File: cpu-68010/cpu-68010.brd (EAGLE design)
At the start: 150 x 100 mm, 84 parts, among them IC10 74HC30D, IC11 74HC30D, IC12 74HC14D, IC13 MAX232, IC6 74HC00D, IC7 74HCT154DW, IC8 74HC04D, IC9 74HC148D, Q1 3.6864MHz, X1 FABC96R

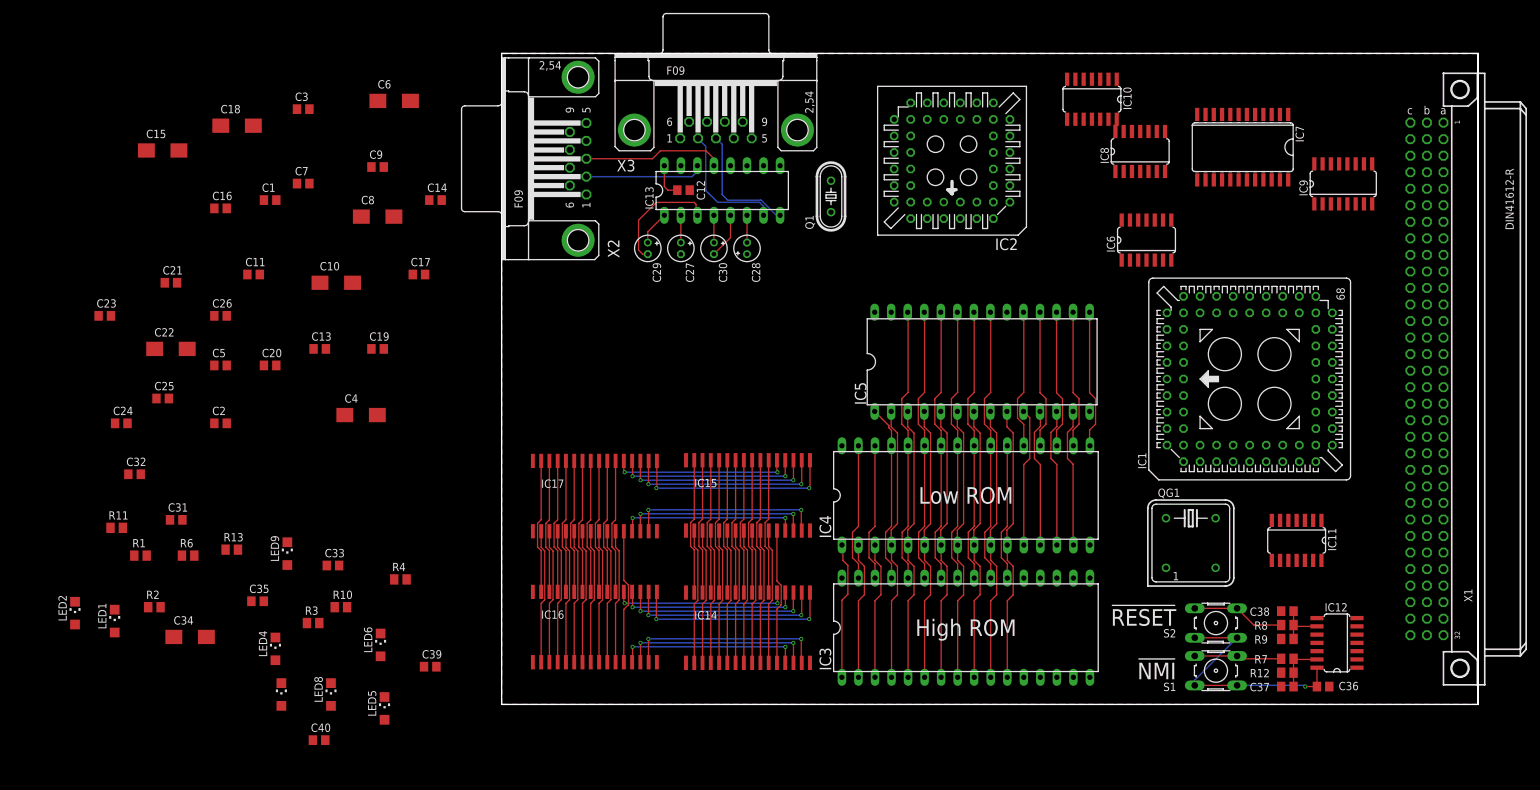
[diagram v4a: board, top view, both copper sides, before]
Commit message: routed remaining signals between SRAM, added decoupling chips and more status LEDs
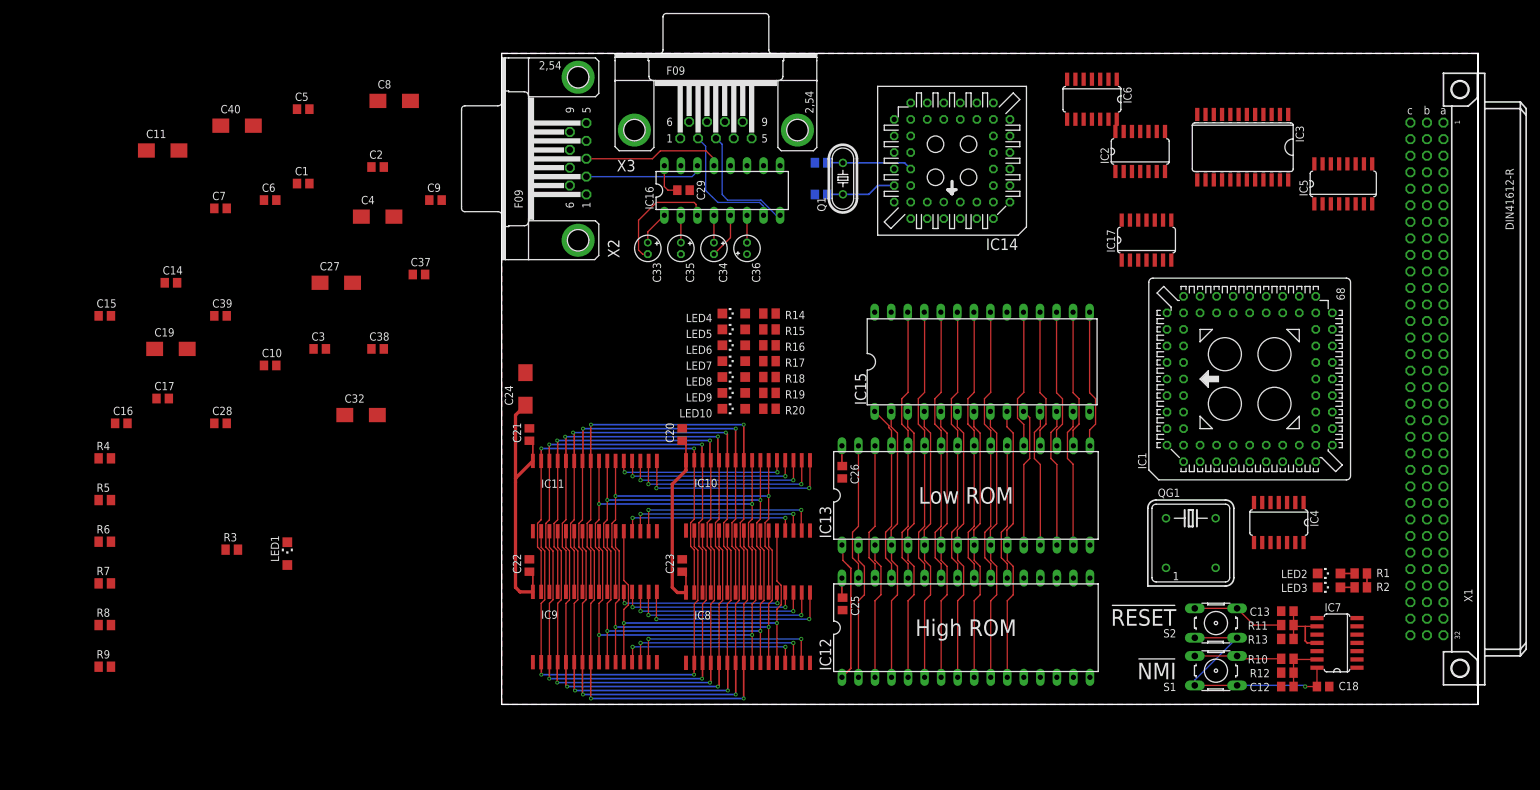
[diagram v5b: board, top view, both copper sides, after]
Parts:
- added LED10, LED7: YEL, led:CHIPLED_1206
- added R14, R15, R16, R17, R18, R19, R20: 680R, rcl:M0805
- added R5: 10k, rcl:M0805
- C10, C15, C18, C22, C6: value 47µF -> 100nF; device rcl:CT6032 -> rcl:C0805
- C11, C19, C24, C40: value 100nF -> 47µF; device rcl:C0805 -> rcl:CT6032
- C27: value 10µF -> 47µF; device rcl:E1,8-4 -> rcl:CT6032
- C28, C29: value 10µF -> 100nF; device rcl:E1,8-4 -> rcl:C0805
- C30: value 10µF -> 30pF; device rcl:E1,8-4 -> rcl:C0805
- C32: value 30pF -> 47µF; device rcl:C0805 -> rcl:CT6032
- C33, C35, C36: value 100nF -> 10µF; device rcl:C0805 -> rcl:E1,8-4
- C34: value 47µF -> 10µF; device rcl:CT6032 -> rcl:E1,8-4
- IC10, IC11: value 74HC30D -> (none); device 74xx-eu:SO14 -> 68komputer:SO32X
- IC12: value 74HC14D -> (none); device 74xx-eu:SO14 -> 68komputer:DIL32
- IC13: value MAX232 -> (none); device maxim:DIL16 -> 68komputer:DIL32
- IC14: device 68komputer:SO32X -> 68komputer:PLCC-S44
- IC15: device 68komputer:SO32X -> 68komputer:DIL28-6
- IC16: value (none) -> MAX232; device 68komputer:SO32X -> maxim:DIL16
- IC17: value (none) -> 74HC00D; device 68komputer:SO32X -> 74xx-eu:SO14
- IC2: value (none) -> 74HC04D; device 68komputer:PLCC-S44 -> 74xx-eu:SO14
- IC3: value (none) -> 74HCT154DW; device 68komputer:DIL32 -> 74xx-eu:SO24W
- IC4: value (none) -> 74HC30D; device 68komputer:DIL32 -> 74xx-eu:SO14
- IC5: value (none) -> 74HC148D; device 68komputer:DIL28-6 -> 74xx-eu:SO16
- IC6: value 74HC00D -> 74HC30D
- IC7: value 74HCT154DW -> 74HC14D; device 74xx-eu:SO24W -> 74xx-eu:SO14
- IC8: value 74HC04D -> (none); device 74xx-eu:SO14 -> 68komputer:SO32X
- IC9: value 74HC148D -> (none); device 74xx-eu:SO16 -> 68komputer:SO32X
- LED2, LED3: value GRN -> RED
- LED4, LED5, LED6, LED8, LED9: value GRN -> YEL
- R10, R11, R13, R4, R6: value 680R -> 10k
- moved LED2 192.7 mm to (127.1, 20.1), turned to 90 degrees
- moved C18 187.8 mm to (126.2, 2.74)
- moved R1 187.5 mm to (132.0, 20.1), turned to 180 degrees
- moved R2 185.3 mm to (132.0, 18.0), turned to 180 degrees
- moved R7 182.0 mm to (-61.0, 18.6), turned to 0 degrees
- moved R9 181.7 mm to (-61.0, 5.79), turned to 0 degrees
- moved R8 181.7 mm to (-61.0, 12.2), turned to 0 degrees
- moved R11 180.5 mm to (120.7, 12.2), turned to 180 degrees
- moved R13 162.7 mm to (120.7, 10.1), turned to 180 degrees
- moved LED3 161.8 mm to (127.1, 18.0), turned to 90 degrees
- moved C13 154.0 mm to (120.7, 14.3), turned to 180 degrees
- moved C37 147.7 mm to (-12.7, 66.0), turned to 0 degrees
- moved R10 145.6 mm to (120.7, 7.01), turned to 180 degrees
- moved C38 145.4 mm to (-19.1, 54.6), turned to 0 degrees
- moved IC9 133.6 mm to (14.3, 11.9)
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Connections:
- new net N$12: LED3.A, R2.2
- new net N$15: LED2.A, R1.2
- net !68681_CS: now also IC14.39, IC17.3; no longer IC2.39, IC6.3
- net !68681_DTACK: now also IC14.10, IC6.2, R9.2; no longer IC10.2, IC2.10
- net !68681_IRQ: now also IC14.24, IC5.2, R5.2; no longer IC2.24, IC9.2
- net !68681_IRQACK: now also IC14.41; no longer IC2.41
- net !A18: now also IC10.30, IC11.30, IC2.10, IC8.30, IC9.30; no longer IC14.30, IC15.30, IC16.30, IC17.30, IC8.10
- net !A19: now also IC17.2, IC2.6; no longer IC6.2, IC8.6
- net !DTACK: now also IC2.8; no longer IC8.8
- net !EXT_DTACK: now also IC6.1, R8.2; no longer IC10.1
- net !EXT_IRQ: now also IC5.1, R4.2; no longer IC9.1
- net !HALT: now also IC7.10, LED2.C
- net !IPL0: now also IC5.9; no longer IC9.9
- net !IPL1: now also IC5.7; no longer IC9.7
- net !IPL2: now also IC5.6; no longer IC9.6
- net !NMI: now also IC5.4, IC7.12, R7.2; no longer IC12.12, IC9.4
- net !OE: now also IC10.24, IC11.24, IC12.24, IC13.24, IC15.22, IC2.2, IC8.24, IC9.24; no longer IC14.24, IC15.24, IC16.24, IC17.24, IC3.24, IC4.24, IC5.22, IC8.2
- net !REGION0: now also IC12.22, IC13.22, IC3.1, IC6.3; no longer IC10.3, IC3.22, IC4.22, IC7.1
- net !REGION1: now also IC10.22, IC11.22, IC3.2, IC6.4, IC8.22, IC9.22; no longer IC10.4, IC14.22, IC15.22, IC16.22, IC17.22, IC7.2
- net !REGION10: now also IC3.11; no longer IC7.11
- net !REGION11: now also IC3.13; no longer IC7.13
- net !REGION12: now also IC3.14; no longer IC7.14
- net !REGION13: now also IC3.15; no longer IC7.15
- net !REGION14: now also IC3.16; no longer IC7.16
- net !REGION15: now also IC2.3, IC3.17; no longer IC7.17, IC8.3
- net !REGION2: now also IC3.3; no longer IC7.3
- net !REGION3: now also IC3.4; no longer IC7.4
- net !REGION4: now also IC3.5; no longer IC7.5
- net !REGION5: now also IC3.6; no longer IC7.6
- net !REGION6: now also IC3.7; no longer IC7.7
- net !REGION7: now also IC3.8; no longer IC7.8
- net !REGION8: now also IC3.9; no longer IC7.9
- net !REGION9: now also IC3.10; no longer IC7.10
- net !RESET: now also IC14.38, IC7.8, LED3.C; no longer IC12.8, IC2.38
- net !RTC_CS: now also IC15.20, IC17.6, IC6.5; no longer IC10.5, IC5.20, IC6.6
- net !TIMER_IRQ: now also IC5.3, R6.2; no longer IC9.3
- net !VPA: now also IC4.8; no longer IC11.8
- net +5V: now also C10.1, C11.+, C15.1, C18.1, C19.+, C22.1, C24.+, C27.+, C28.1, C29.1, C32.+, C35.-, C37.1, C38.1, C40.+, C6.1, IC10.32, IC11.32, IC12.32, IC13.32, IC14.44, IC15.28, IC16.16, IC17.14, IC2.14, IC3.24, IC4.12, IC4.14, IC5.11, IC5.12, IC5.13, IC5.16, IC6.11, IC6.12, IC6.6, IC7.14, IC8.32, IC9.32, R1.1, R2.1, R3.1, R4.1, R8.1, R9.1; no longer C10.+, C11.1, C12.1, C13.1, C15.+, C18.+, C19.1, C22.+, C24.1, C27.-, C33.1, C34.+, C35.1, C36.1, C40.1, C6.+, IC10.11, IC10.12, IC10.14, IC10.6, IC11.12, IC11.14, IC12.14, IC13.16, IC14.32, IC15.32, IC16.32, IC17.32, IC2.44, IC3.32, IC4.32, IC5.28, IC7.24, IC8.14, IC9.11, IC9.12, IC9.13, IC9.16, R13.1
- net /AS: now also IC3.18, IC3.19; no longer IC7.18, IC7.19
- net 68681_XTAL1: now also C30.1, IC14.36; no longer C31.1, IC2.36
- net 68681_XTAL2: now also C31.2, IC14.37; no longer C32.2, IC2.37
- net A1: now also IC10.12, IC11.12, IC12.12, IC13.12, IC14.2, IC15.10, IC8.12, IC9.12; no longer IC14.12, IC15.12, IC16.12, IC17.12, IC2.2, IC3.12, IC4.12, IC5.10
- net A10: now also IC10.26, IC11.26, IC12.26, IC13.26, IC15.24, IC8.26, IC9.26; no longer IC14.26, IC15.26, IC16.26, IC17.26, IC3.26, IC4.26, IC5.24
- net A11: now also IC10.23, IC11.23, IC12.23, IC13.23, IC15.21, IC8.23, IC9.23; no longer IC14.23, IC15.23, IC16.23, IC17.23, IC3.23, IC4.23, IC5.21
- net A12: now also IC10.25, IC11.25, IC12.25, IC13.25, IC15.23, IC8.25, IC9.25; no longer IC14.25, IC15.25, IC16.25, IC17.25, IC3.25, IC4.25, IC5.23
- net A13: now also IC10.4, IC11.4, IC12.4, IC13.4, IC15.2, IC8.4, IC9.4; no longer IC14.4, IC15.4, IC16.4, IC17.4, IC3.4, IC4.4, IC5.2
- net A14: now also IC10.28, IC11.28, IC12.28, IC13.28, IC15.26, IC8.28, IC9.28; no longer IC14.28, IC15.28, IC16.28, IC17.28, IC3.28, IC4.28, IC5.26
- net A15: now also IC10.3, IC11.3, IC12.29, IC13.29, IC15.1, IC8.3, IC9.3; no longer IC14.3, IC15.3, IC16.3, IC17.3, IC3.29, IC4.29, IC5.1
- net A16: now also IC10.31, IC11.31, IC12.3, IC13.3, IC4.4, IC8.31, IC9.31; no longer IC11.4, IC14.31, IC15.31, IC16.31, IC17.31, IC3.3, IC4.3
- net A17: now also IC10.2, IC11.2, IC12.2, IC13.2, IC4.5, IC8.2, IC9.2; no longer IC11.5, IC14.2, IC15.2, IC16.2, IC17.2, IC3.2, IC4.2
- net A18: now also IC12.30, IC13.30, IC2.11, IC4.6; no longer IC11.6, IC3.30, IC4.30, IC8.11
- net A19: now also IC12.1, IC13.1, IC17.5, IC2.5, IC4.11; no longer IC11.11, IC3.1, IC4.1, IC6.5, IC8.5
- net A2: now also IC10.11, IC11.11, IC12.11, IC13.11, IC14.4, IC15.9, IC8.11, IC9.11; no longer IC14.11, IC15.11, IC16.11, IC17.11, IC2.4, IC3.11, IC4.11, IC5.9
- net A20: now also IC3.23; no longer IC7.23
- net A21: now also IC3.22; no longer IC7.22
- net A22: now also IC3.21; no longer IC7.21
- net A23: now also IC3.20; no longer IC7.20
- net A3: now also IC10.10, IC11.10, IC12.10, IC13.10, IC14.6, IC15.8, IC8.10, IC9.10; no longer IC14.10, IC15.10, IC16.10, IC17.10, IC2.6, IC3.10, IC4.10, IC5.8
- net A4: now also IC10.9, IC11.9, IC12.9, IC13.9, IC14.7, IC15.7, IC8.9, IC9.9; no longer IC14.9, IC15.9, IC16.9, IC17.9, IC2.7, IC3.9, IC4.9, IC5.7
- net A5: now also IC10.8, IC11.8, IC12.8, IC13.8, IC15.6, IC8.8, IC9.8; no longer IC14.8, IC15.8, IC16.8, IC17.8, IC3.8, IC4.8, IC5.6
- net A6: now also IC10.7, IC11.7, IC12.7, IC13.7, IC15.5, IC8.7, IC9.7; no longer IC14.7, IC15.7, IC16.7, IC17.7, IC3.7, IC4.7, IC5.5
- net A7: now also IC10.6, IC11.6, IC12.6, IC13.6, IC15.4, IC8.6, IC9.6; no longer IC14.6, IC15.6, IC16.6, IC17.6, IC3.6, IC4.6, IC5.4
- net A8: now also IC10.5, IC11.5, IC12.5, IC13.5, IC15.3, IC8.5, IC9.5; no longer IC14.5, IC15.5, IC16.5, IC17.5, IC3.5, IC4.5, IC5.3
- net A9: now also IC10.27, IC11.27, IC12.27, IC13.27, IC15.25, IC8.27, IC9.27; no longer IC14.27, IC15.27, IC16.27, IC17.27, IC3.27, IC4.27, IC5.25
- net D0: now also IC10.13, IC11.13, IC13.13, IC14.28, IC15.11; no longer IC15.13, IC17.13, IC2.28, IC4.13, IC5.11
- net D1: now also IC10.14, IC11.14, IC13.14, IC14.18, IC15.12; no longer IC15.14, IC17.14, IC2.18, IC4.14, IC5.12
- net D10: now also IC12.15, IC8.15, IC9.15; no longer IC14.15, IC16.15, IC3.15
- net D11: now also IC12.17, IC8.17, IC9.17; no longer IC14.17, IC16.17, IC3.17
- net D12: now also IC12.18, IC8.18, IC9.18; no longer IC14.18, IC16.18, IC3.18
- net D13: now also IC12.19, IC8.19, IC9.19; no longer IC14.19, IC16.19, IC3.19
- net D14: now also IC12.20, IC8.20, IC9.20; no longer IC14.20, IC16.20, IC3.20
- net D15: now also IC12.21, IC8.21, IC9.21; no longer IC14.21, IC16.21, IC3.21
- net D2: now also IC10.15, IC11.15, IC13.15, IC14.27, IC15.13; no longer IC15.15, IC17.15, IC2.27, IC4.15, IC5.13
- net D3: now also IC10.17, IC11.17, IC13.17, IC14.19, IC15.15; no longer IC15.17, IC17.17, IC2.19, IC4.17, IC5.15
- net D4: now also IC10.18, IC11.18, IC13.18, IC14.26, IC15.16; no longer IC15.18, IC17.18, IC2.26, IC4.18, IC5.16
- net D5: now also IC10.19, IC11.19, IC13.19, IC14.20, IC15.17; no longer IC15.19, IC17.19, IC2.20, IC4.19, IC5.17
- net D6: now also IC10.20, IC11.20, IC13.20, IC14.25, IC15.18; no longer IC15.20, IC17.20, IC2.25, IC4.20, IC5.18
- net D7: now also IC10.21, IC11.21, IC13.21, IC14.21, IC15.19; no longer IC15.21, IC17.21, IC2.21, IC4.21, IC5.19
- net D8: now also IC12.13, IC8.13, IC9.13; no longer IC14.13, IC16.13, IC3.13
- net D9: now also IC12.14, IC8.14, IC9.14; no longer IC14.14, IC16.14, IC3.14
- net DTACK: now also IC2.9, IC6.8; no longer IC10.8, IC8.9
- net FC0: now also IC4.1; no longer IC11.1
- net FC1: now also IC4.2; no longer IC11.2
- net FC2: now also IC4.3; no longer IC11.3
- net GND: now also C10.2, C11.-, C15.2, C18.2, C19.-, C22.2, C24.-, C27.-, C28.2, C29.2, C30.2, C31.1, C32.-, C36.+, C40.-, C6.2, IC10.16, IC11.16, IC12.16, IC13.16, IC14.22, IC15.14, IC16.15, IC17.7, IC2.7, IC3.12, IC4.7, IC5.10, IC5.5, IC5.8, IC7.7, IC8.16, IC9.16, LED1.C, LED10.C, LED4.C, LED5.C, LED7.C, R13.2; no longer C10.-, C11.2, C15.-, C18.-, C19.2, C22.-, C24.2, C28.+, C31.2, C32.1, C33.2, C34.-, C35.2, C36.2, C40.2, C6.-, IC10.7, IC11.7, IC12.7, IC13.15, IC14.16, IC15.16, IC16.16, IC17.16, IC2.22, IC3.16, IC4.16, IC5.14, IC7.12, IC8.7, IC9.10, IC9.5, IC9.8, R9.2
- net GPIO_IN0: now also IC14.8; no longer IC2.8
- net GPIO_IN1: now also IC14.5; no longer IC2.5
- net GPIO_IN2: now also IC14.40; no longer IC2.40
- net GPIO_IN3: now also IC14.3; no longer IC2.3
- net GPIO_IN4: now also IC14.43; no longer IC2.43
- net GPIO_IN5: now also IC14.42; no longer IC2.42
- net GPIO_OUT0: now also IC14.32, R14.1; no longer IC2.32, R4.1
- net GPIO_OUT1: now also IC14.14, R15.1; no longer IC2.14, R3.1
- net GPIO_OUT2: now also IC14.15, R16.1; no longer IC2.15, R2.1
- net GPIO_OUT3: now also IC14.30, R17.1; no longer IC2.30, R1.1
- net GPIO_OUT4: now also IC14.16, R18.1; no longer IC2.16, R11.1
- net GPIO_OUT5: now also IC14.29, R19.1; no longer IC2.29, R10.1
- net GPIO_OUT6: now also IC14.17, R20.1; no longer IC2.17, R6.1
- net N$1: now also C35.+, IC16.2; no longer C27.+, IC13.2
- net N$10: now also LED7.A, R17.2; no longer LED1.A, R1.2
- net N$11: now also LED6.A, R16.2; no longer LED2.A, R2.2
- net N$13: now also R15.2; no longer R3.2
- net N$14: now also LED4.A, R14.2; no longer LED6.A, R4.2
- net N$17: now also LED10.A, R20.2; no longer LED8.A, R6.2
- net N$18: now also R10.2; no longer R7.2
- net N$19: now also LED1.A, R3.2; no longer LED9.A, R13.2
- net N$2: now also C36.-, IC16.6; no longer C28.-, IC13.6
- net N$3: now also C33.+, IC16.1; no longer C29.+, IC13.1
- net N$4: now also C34.+, IC16.4; no longer C30.+, IC13.4
- net N$5: now also C33.-, IC16.3; no longer C29.-, IC13.3
- net N$6: now also C34.-, IC16.5; no longer C30.-, IC13.5
- net N$7: now also LED9.A, R19.2; no longer LED3.A, R10.2
- net N$8: now also LED8.A, R18.2; no longer LED4.A, R11.2
- net N$9: now also R11.2; no longer R8.2
- net NMI_SW: now also C12.1, IC7.13, R10.1; no longer C37.1, IC12.13, R7.1
- net R!W!: now also IC2.1; no longer IC8.1
- net R/!W!: now also IC10.29, IC11.29, IC12.31, IC13.31, IC14.9, IC15.27, IC8.29, IC9.29; no longer IC14.29, IC15.29, IC16.29, IC17.29, IC2.9, IC3.31, IC4.31, IC5.27
- net REGION15: now also IC17.1, IC17.4, IC2.4; no longer IC6.1, IC6.4, IC8.4
- net RESET_SW: now also C13.1, IC7.11, IC7.9, R11.1, R13.1; no longer C38.1, IC12.9, R8.1, R9.1
- net RS232_0_RX: now also IC16.14; no longer IC13.14
- net RS232_0_TX: now also IC16.13; no longer IC13.13
- net RS232_1_RX: now also IC16.7; no longer IC13.7
- net RS232_1_TX: now also IC16.8; no longer IC13.8
- net TIMER_CLK: now also IC14.31; no longer IC2.31
- net UART0_RX: now also IC14.35, IC16.12; no longer IC13.12, IC2.35
- net UART0_TX: now also IC14.33, IC16.11; no longer IC13.11, IC2.33
- net UART1_RX: now also IC14.11, IC16.9; no longer IC13.9, IC2.11
- net UART1_TX: now also IC14.13, IC16.10; no longer IC13.10, IC2.13
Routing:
- net +5V: track 43.7 -> 123.5 mm
- net A12: track 83.8 -> 118.3 mm, vias 0 -> 2
- net A5: track 83.9 -> 118.4 mm, vias 0 -> 2
- net A10: track 83.8 -> 117.4 mm, vias 0 -> 2
- net A6: track 83.9 -> 117.2 mm, vias 0 -> 2
- net A9: track 83.8 -> 116.0 mm, vias 0 -> 2
- net A7: track 83.8 -> 115.9 mm, vias 0 -> 2
- net A14: track 83.8 -> 115.4 mm, vias 0 -> 2
- net A8: track 84.2 -> 114.9 mm, vias 0 -> 2
- net R/!W!: track 62.4 -> 92.2 mm, vias 0 -> 2
- net A13: track 83.8 -> 113.5 mm, vias 0 -> 2
- net A15: track 68.8 -> 97.6 mm, vias 0 -> 2
- net !A18: track 41.4 -> 69.8 mm, vias 0 -> 2
- net A16: track 62.4 -> 89.7 mm, vias 0 -> 2
- net A17: track 62.4 -> 89.7 mm, vias 0 -> 2
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
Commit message: routed more of the address/data busses for ROMs and RAMs
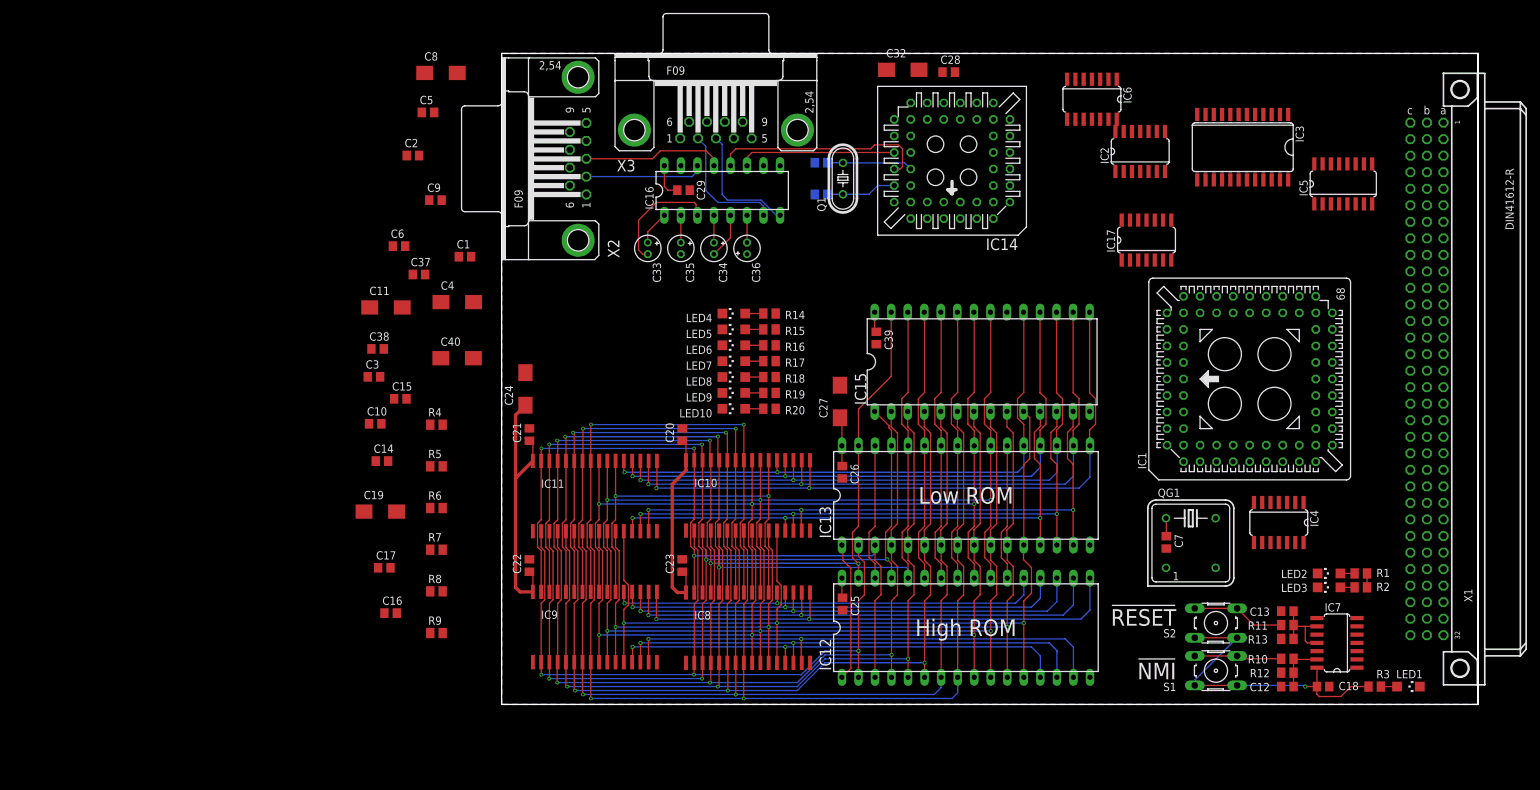
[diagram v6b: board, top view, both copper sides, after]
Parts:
- moved R3 176.8 mm to (134.1, 2.74)
- moved LED1 173.4 mm to (139.3, 2.74), turned to 270 degrees
- moved C7 154.1 mm to (102.1, 24.9), turned to 270 degrees
- moved C28 124.2 mm to (68.7, 97.1)
- moved C39 100.8 mm to (57.6, 56.3), turned to 270 degrees
- moved C32 98.7 mm to (61.6, 97.5)
- moved C27 79.5 mm to (52.0, 46.5), turned to 90 degrees
- moved R4 51.2 mm to (-10.0, 43.0)
- moved R5 51.2 mm to (-10.0, 36.6)
- moved R6 51.2 mm to (-10.0, 30.2)
- moved R7 51.2 mm to (-10.0, 23.8)
- moved R8 51.2 mm to (-10.0, 17.4)
- moved R9 51.2 mm to (-10.0, 11.0)
- moved C16 50.6 mm to (-17.1, 14.0)
- moved C40 49.2 mm to (-6.84, 53.2)
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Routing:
- net A1: track 86.4 -> 145.6 mm, vias 2 -> 3
- net D3: track 53.3 -> 102.0 mm
- net D11: track 31.8 -> 80.4 mm
- net D4: track 52.1 -> 99.0 mm
- net D10: track 30.8 -> 77.7 mm
- net D12: track 30.6 -> 77.1 mm
- net R/!W!: track 92.2 -> 137.6 mm, vias 2 -> 4
- net D9: track 30.9 -> 76.0 mm
- net D5: track 50.8 -> 95.9 mm
- net D13: track 30.2 -> 74.9 mm
- net D6: track 49.6 -> 92.7 mm
- net D8: track 28.3 -> 71.4 mm
- net D14: track 28.1 -> 70.9 mm
- net D2: track 51.2 -> 93.0 mm, vias 2 -> 3
- net D7: track 48.5 -> 89.8 mm
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
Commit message: routed more signals, added power connector
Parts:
- added SV1: 1792863, 68komputer:1792863
- R1, R14, R15, R16, R17, R18, R19, R2, R20, R3: value 680R -> 2k
- moved IC17 26.5 mm to (123.6, 81.4), turned to 270 degrees
- moved IC5 14.0 mm to (123.6, 92.8), turned to 270 degrees
- moved R15 9.42 mm to (31.9, 59.5)
- moved R16 9.42 mm to (31.9, 57.0)
- moved R20 9.42 mm to (31.9, 47.3)
- moved R14 9.42 mm to (31.9, 61.9)
- moved R17 9.42 mm to (31.9, 54.6)
- moved R18 9.42 mm to (31.9, 52.2)
- moved R19 9.42 mm to (31.9, 49.7)
- moved LED10 9.42 mm to (26.4, 47.3)
- moved LED5 9.42 mm to (26.4, 59.5)
- moved LED6 9.42 mm to (26.4, 57.0)
- moved LED4 9.42 mm to (26.4, 61.9)
- moved LED7 9.42 mm to (26.4, 54.6)
- moved LED8 9.42 mm to (26.4, 52.2)
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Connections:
- net +5V: now also SV1.2
- net GND: now also IC2.13, IC7.5, SV1.1
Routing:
- net +5V: track 143.7 -> 312.3 mm
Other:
- board text added: "+5V In"
